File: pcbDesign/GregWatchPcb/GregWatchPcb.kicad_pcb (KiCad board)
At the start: 2 copper layers, 35 parts, among them J1 AVR-ISP-6, SW1 SW_Push, SW2 SW_Push, SW3 SW_Push, SW4 SW_Push, U1 Nokia_5110_LCD, U2 ATmega328P-AU, U3 74HC14, Y1 16M

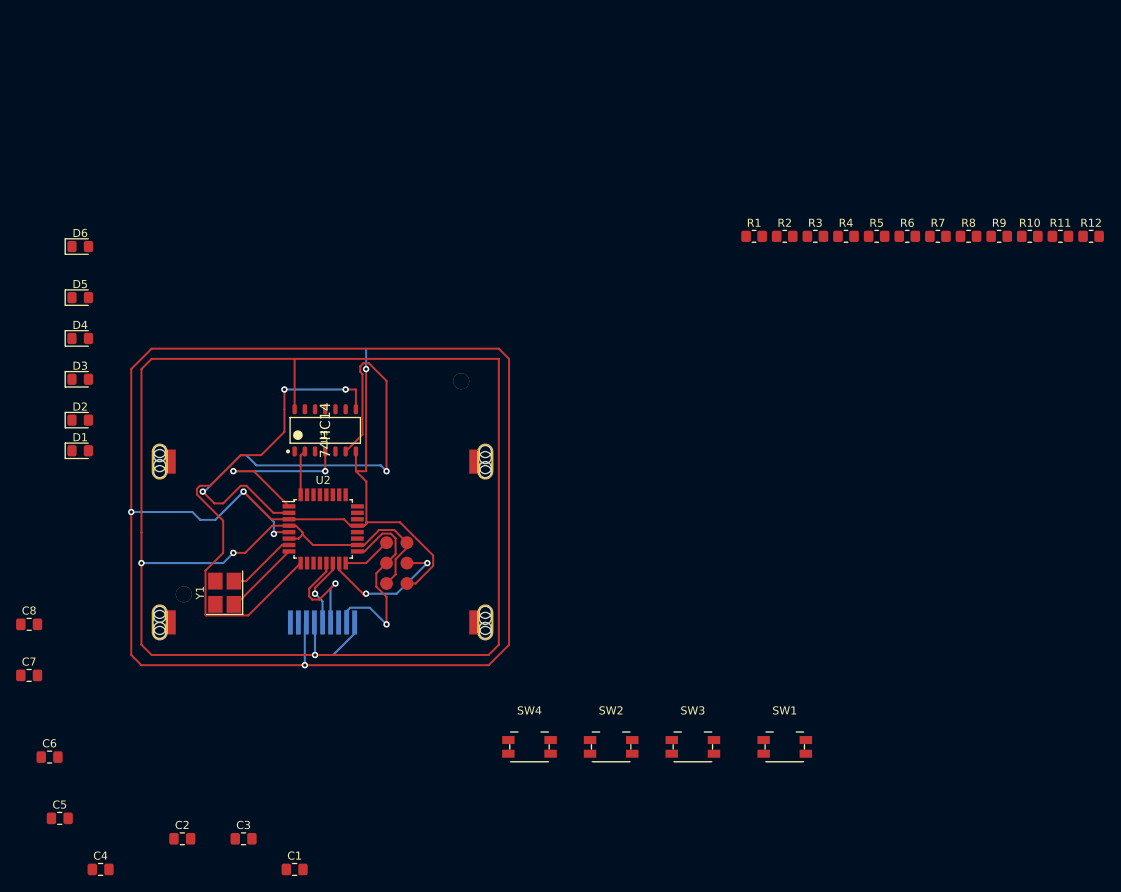
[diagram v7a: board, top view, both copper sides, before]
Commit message: Placed all components. No traces yet.
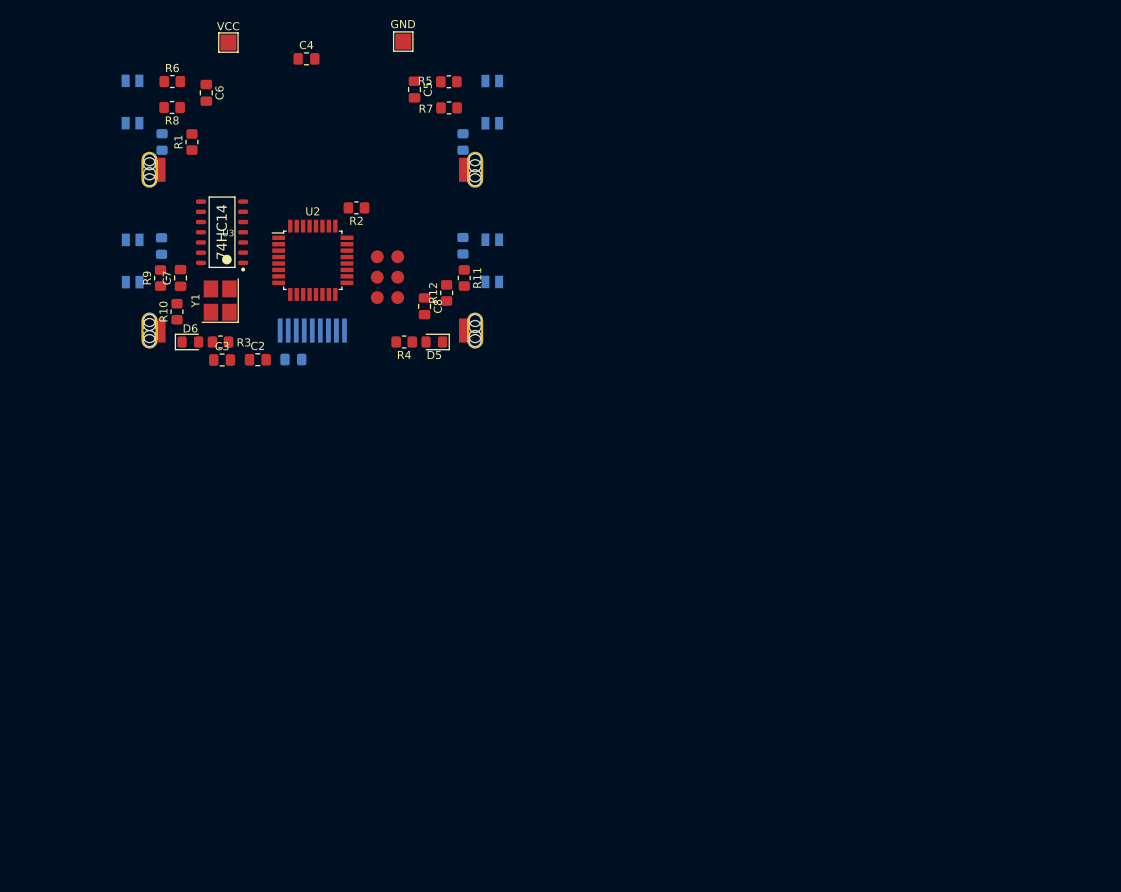
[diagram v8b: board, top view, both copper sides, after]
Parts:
- added GND: TestPoint_Pad_2.0x2.0mm, TestPoint:TestPoint_Pad_2.0x2.0mm, F.Cu at (149.4, 26.6)
- added VCC: TestPoint_Pad_2.0x2.0mm, TestPoint:TestPoint_Pad_2.0x2.0mm, F.Cu at (127.7, 26.7)
- C1, D1, D2, D3, D4, SW1, SW2, SW3, SW4: moved to B.Cu
- moved R10 106.5 mm to (121.3, 60.2), turned to 90 degrees
- moved R9 104.4 mm to (119.2, 56.0), turned to 90 degrees
- moved C4 104.0 mm to (137.4, 28.7)
- moved C5 100.8 mm to (150.8, 32.5), turned to 270 degrees
- moved R8 100.3 mm to (120.7, 34.8), turned to 180 degrees
- moved SW2 99.9 mm to (115.7, 34.1), turned to 270 degrees
- moved R6 93.4 mm to (120.7, 31.6)
- moved SW3 92.2 mm to (115.8, 53.9), turned to 270 degrees
- moved SW1 88.1 mm to (160.5, 34.1), turned to 90 degrees
- moved C6 84.9 mm to (124.9, 33.0), turned to 270 degrees
- moved R12 80.5 mm to (154.8, 57.8), turned to 90 degrees
- moved R3 75.1 mm to (126.7, 63.9)
- moved R11 74.3 mm to (157.0, 56.0), turned to 270 degrees
- moved R1 70.9 mm to (123.1, 39.1), turned to 90 degrees
- moved C1 63.4 mm to (135.7, 66.1), turned to 180 degrees
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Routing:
- net GND: track 256.9 -> 0.00 mm, vias 5 -> 0
- net +5V: track 223.7 -> 0.00 mm, vias 3 -> 0
- net Net-(U2-Pad2): track 66.3 -> 0.00 mm, vias 2 -> 0
- net Net-(U2-Pad9): track 62.9 -> 0.00 mm, vias 2 -> 0
- net Net-(J1-Pad3): track 25.5 -> 0.00 mm, vias 1 -> 0
- net Net-(U2-Pad1): track 22.6 -> 0.00 mm, vias 2 -> 0
- net Net-(J1-Pad4): track 17.2 -> 0.00 mm, vias 2 -> 0
- net Net-(U1-Pad6): track 14.4 -> 0.00 mm, vias 1 -> 0
- net Net-(C3-Pad2): track 9.59 -> 0.00 mm
- net Net-(C2-Pad2): track 8.72 -> 0.00 mm
- net Net-(U1-Pad5): track 8.68 -> 0.00 mm, vias 1 -> 0
- net Net-(J1-Pad1): track 6.13 -> 0.00 mm
- net Net-(U2-Pad32): track 5.60 -> 0.00 mm
